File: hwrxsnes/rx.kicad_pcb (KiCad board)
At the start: 2 copper layers, 28.4 x 18.7 mm, 20 parts, among them IC1 ATMEGA328-A, P1 +5v, P2 Clock, P3 Latch, P4 Data, P5 GND, P6 nRF, P7 ISP, P8 RX, P9 TX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

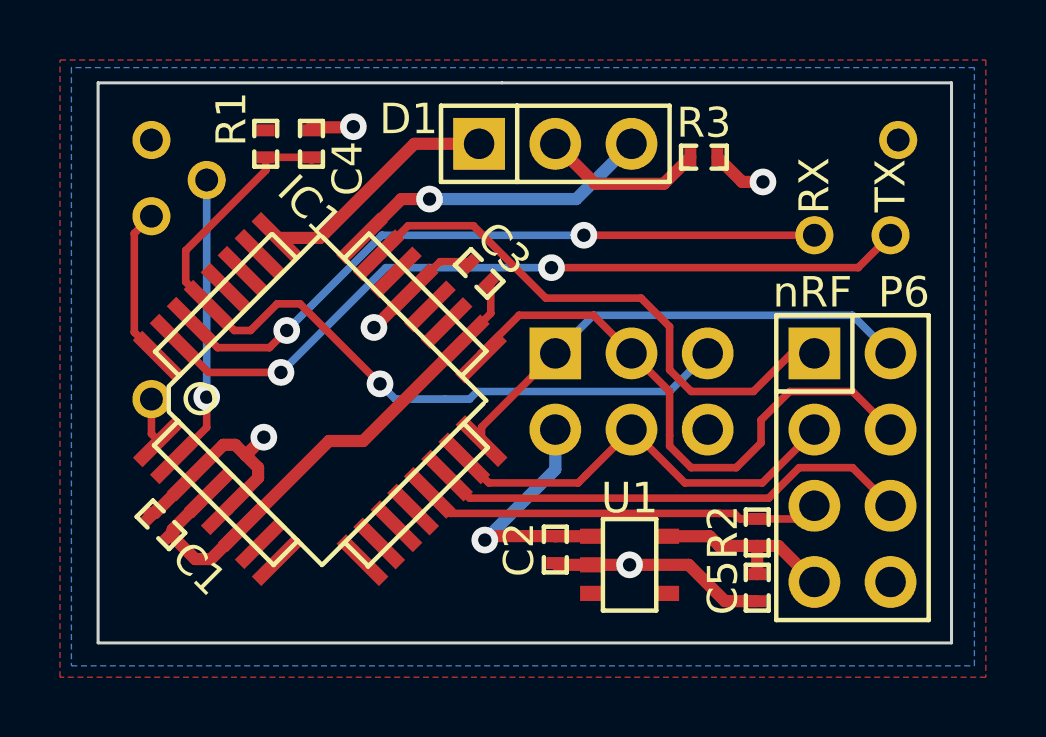
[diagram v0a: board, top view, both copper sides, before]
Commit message: v2
* Schematic revs:
  * TVS protection on TX
  * TX voltage divider moved after the power switch
  * RX adds crystal to run at 16MHz
RX software tested w/ a real console.
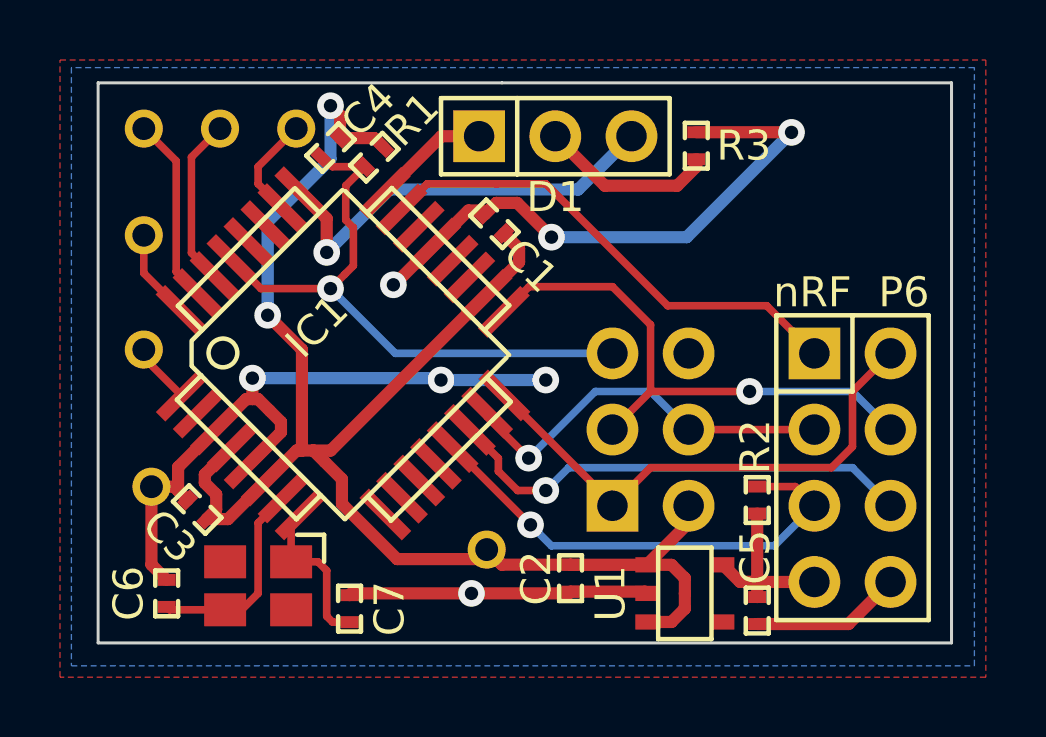
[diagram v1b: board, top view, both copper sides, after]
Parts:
- added C6: 22p, SMD_Packages:SMD-0402_c, F.Cu at (129.3, 93.2)
- added C7: 22p, SMD_Packages:SMD-0402_c, F.Cu at (135.4, 93.7)
- added X1: CRYSTAL, TSX-3225, F.Cu at (132.3, 93.0)
- P8, P9: moved to B.Cu
- moved P5 27.4 mm to (128.8, 89.7), turned to 45 degrees
- moved P9 25.1 mm to (128.5, 77.7)
- moved P8 20.1 mm to (131.1, 77.7)
- moved P1 17.6 mm to (140.0, 91.8)
- moved C1 15.0 mm to (140.2, 80.9)
- moved C3 12.3 mm to (130.3, 90.4)
- moved R1 3.65 mm to (136.2, 78.7), turned to 45 degrees
- moved P4 3.44 mm to (133.6, 77.7)
- moved U1 2.07 mm to (146.6, 93.2)
- moved IC1 1.70 mm to (135.2, 85.2)
- moved P2 1.67 mm to (128.5, 85.1)
- moved P7 1.42 mm to (145.4, 87.8), turned to 90 degrees
- moved R2 1.08 mm to (149.0, 90.1)
- moved C2 1.08 mm to (142.7, 92.7)
- moved C5 0.76 mm to (149.0, 93.8)
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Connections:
- C4 pad 1: GND -> /~RST
- C4 pad 2: /~RST -> +5V
- IC1 pad 10: Net-(IC1-Pad10) -> (no net)
- IC1 pad 11: Net-(IC1-Pad11) -> (no net)
- IC1 pad 12: Net-(IC1-Pad12) -> (no net)
- IC1 pad 19: Net-(IC1-Pad19) -> (no net)
- IC1 pad 2: /Data -> (no net)
- IC1 pad 20: Net-(IC1-Pad20) -> (no net)
- IC1 pad 22: Net-(IC1-Pad22) -> (no net)
- IC1 pad 24: /Yellow -> /Green
- IC1 pad 25: /Green -> /Yellow
- IC1 pad 26: Net-(IC1-Pad26) -> /Data
- IC1 pad 27: Net-(IC1-Pad27) -> (no net)
- IC1 pad 28: Net-(IC1-Pad28) -> (no net)
- IC1 pad 7: Net-(IC1-Pad7) -> /XTAL1
- IC1 pad 8: Net-(IC1-Pad8) -> /XTAL2
- IC1 pad 9: Net-(IC1-Pad9) -> (no net)
- U1 pad 4: Net-(U1-Pad4) -> (no net)
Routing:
- net GND: track 22.8 -> 57.4 mm, vias 5 -> 7
- net +5V: track 25.5 -> 53.9 mm, vias 1 -> 2
- net /SER_TX: track 26.2 -> 6.27 mm, vias 2 -> 0
- net /SER_RX: track 22.6 -> 5.67 mm, vias 2 -> 0
- net /XTAL1: track 0.00 -> 7.00 mm
- net /~RST: track 27.2 -> 20.2 mm
- net /Data: track 9.70 -> 3.56 mm, vias 1 -> 0
- net /XTAL2: track 0.00 -> 5.52 mm
- net /Green: track 8.02 -> 3.93 mm
- net /Yellow: track 10.3 -> 14.1 mm
- net /RF_CSN: track 13.4 -> 16.1 mm, vias 0 -> 1
- net /Latch: track 5.25 -> 3.04 mm
- net /RF_IRQ: track 18.6 -> 16.5 mm
- net /MISO: track 16.3 -> 17.6 mm
- net /SCK: track 19.6 -> 18.3 mm, vias 0 -> 1
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- added copper zone on F.Cu, net GND
- removed copper zone on F.Cu, net +5V
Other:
- rule trace_min: 0.01 -> 0.254
- rule via_min_size: 0.035 -> 0.889
- board text added: "ISP"
- board text added: "nesRF SNES Receiver arantius.com Jan 2015"
- board text removed: "nesRF SNES Receiver arantius.com Dec 2014"

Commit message: end-to-end working on breadboard
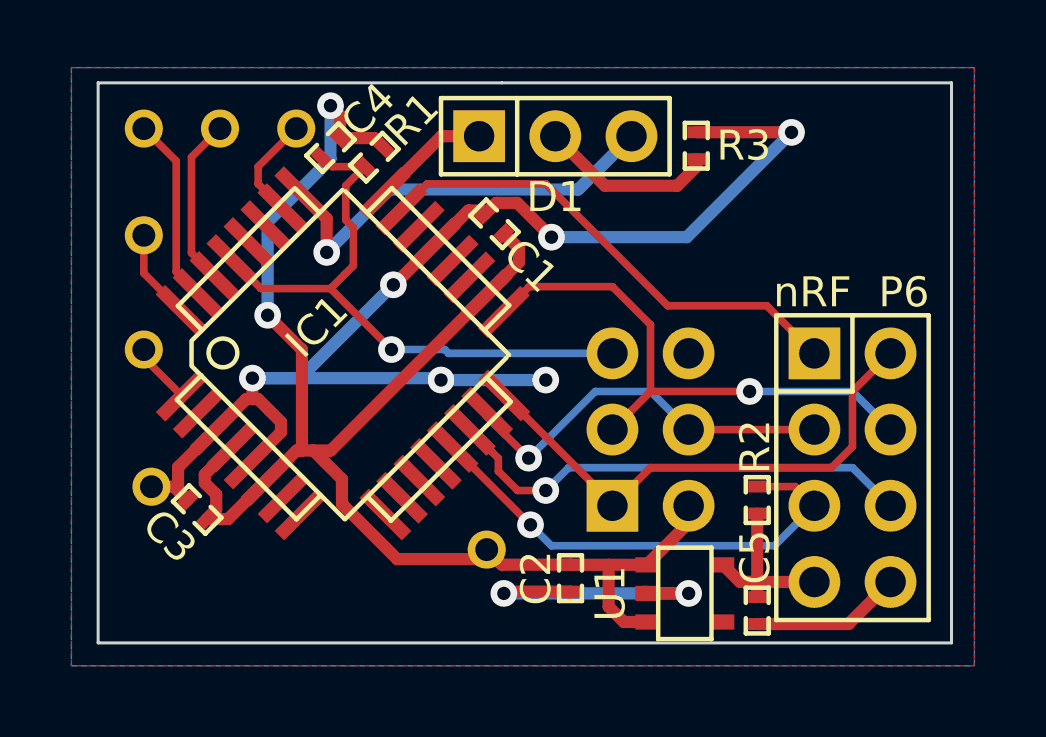
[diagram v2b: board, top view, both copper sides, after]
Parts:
- removed C6, C7: 22p, SMD_Packages:SMD-0402_c
- removed X1: CRYSTAL, TSX-3225
- C2: value 1u -> 0.1u
- R3: value 120 -> 180
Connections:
- IC1 pad 7: /XTAL1 -> (no net)
- IC1 pad 8: /XTAL2 -> (no net)
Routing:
- net /XTAL1: track 7.00 -> 0.00 mm
- net /XTAL2: track 5.52 -> 0.00 mm
- net GND: track 57.4 -> 60.0 mm, vias 7 -> 8
- net +5V: track 53.9 -> 52.8 mm

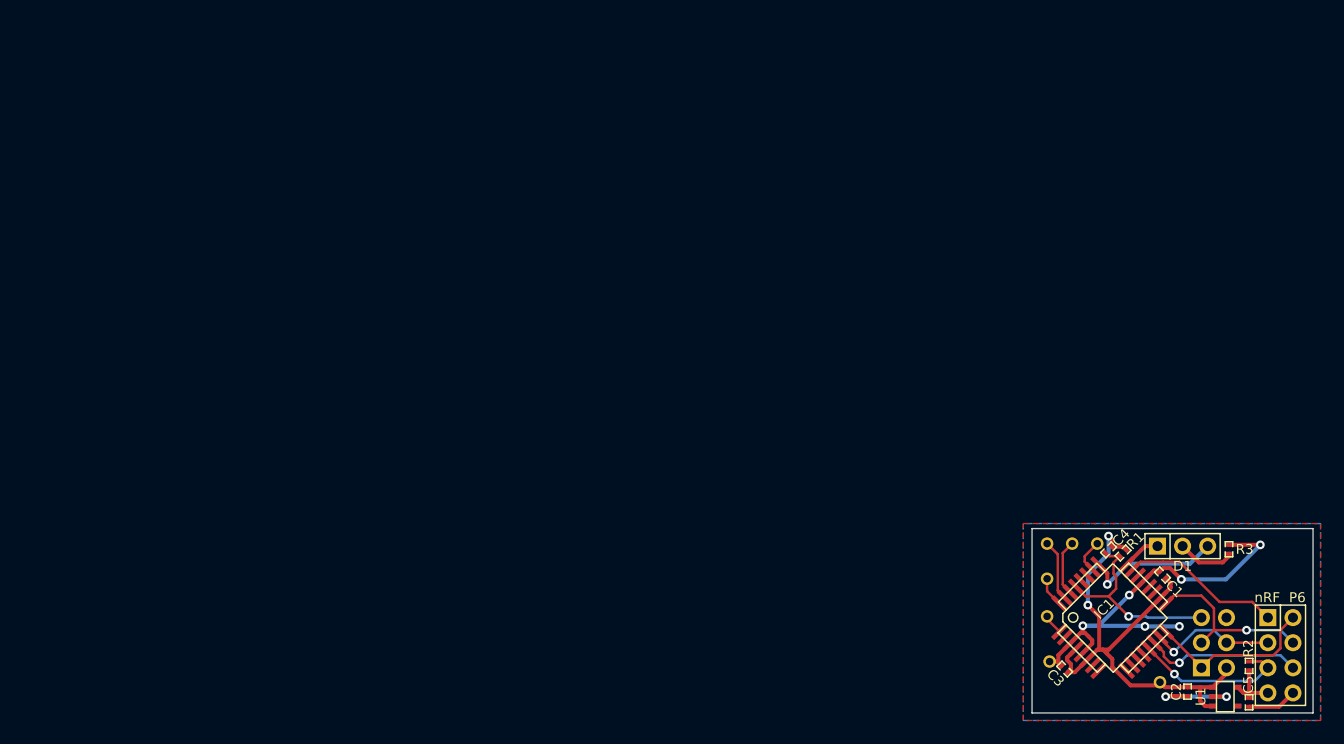
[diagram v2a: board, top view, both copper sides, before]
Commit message: finalize TX for SNES
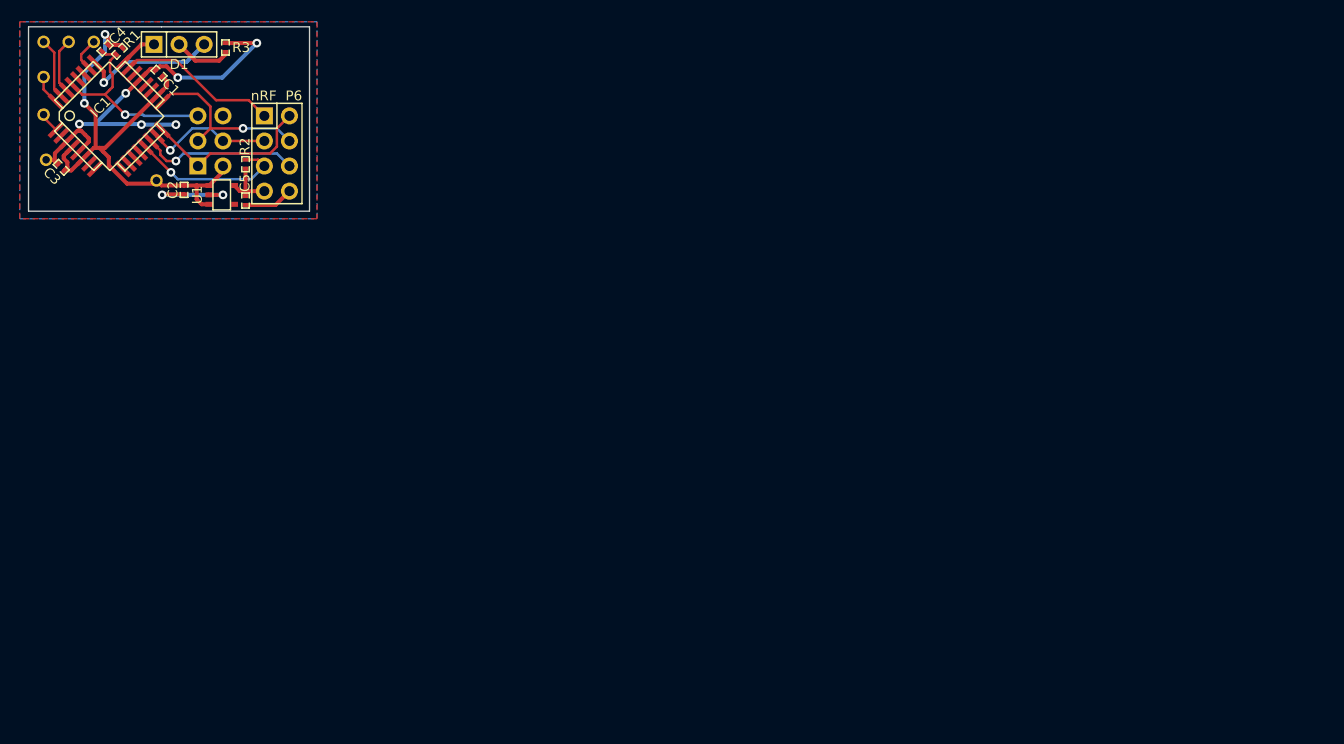
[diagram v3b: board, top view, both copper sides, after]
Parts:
- moved P4 113.6 mm to (32.0, 26.9)
- moved D1 113.6 mm to (40.6, 27.2)
- moved R1 113.6 mm to (34.6, 27.9)
- moved C4 113.6 mm to (33.1, 27.6)
- moved C1 113.6 mm to (38.6, 30.1)
- moved C2 113.6 mm to (41.1, 41.9)
- moved C3 113.6 mm to (28.7, 39.6)
- moved C5 113.6 mm to (47.4, 43.0)
- moved IC1 113.6 mm to (33.6, 34.4)
- moved P1 113.6 mm to (38.4, 41.0)
- moved P2 113.6 mm to (26.9, 34.3)
- moved P3 113.6 mm to (26.9, 30.5)
- moved P5 113.6 mm to (27.2, 38.9)
- moved P6 113.6 mm to (50.5, 38.2)
- moved P7 113.6 mm to (43.8, 37.0)
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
